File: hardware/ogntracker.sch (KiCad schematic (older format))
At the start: 53 parts, among them J1 ANT, J2 SWD, J3 BOOT, SW1 RESET, U1 LM2936-3.3, Y1 32.768K, Y2 8MHz

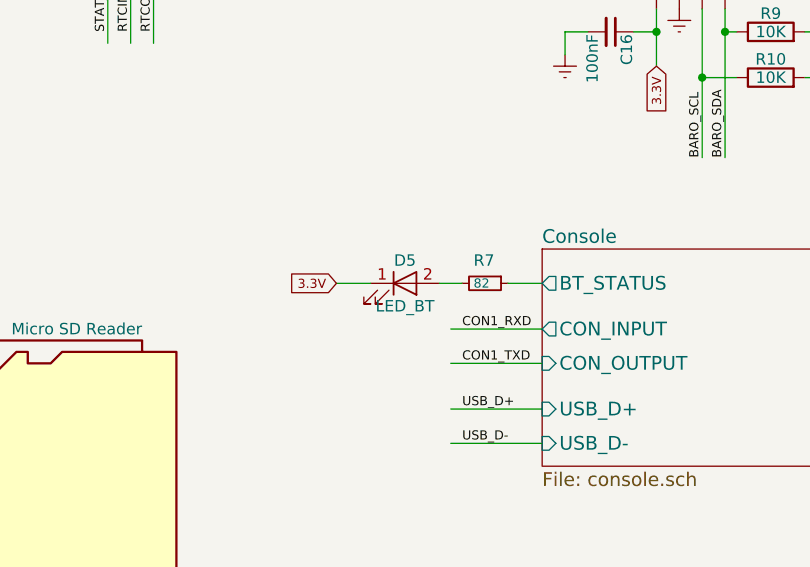
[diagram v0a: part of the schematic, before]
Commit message: All the used footprints moved to project directory
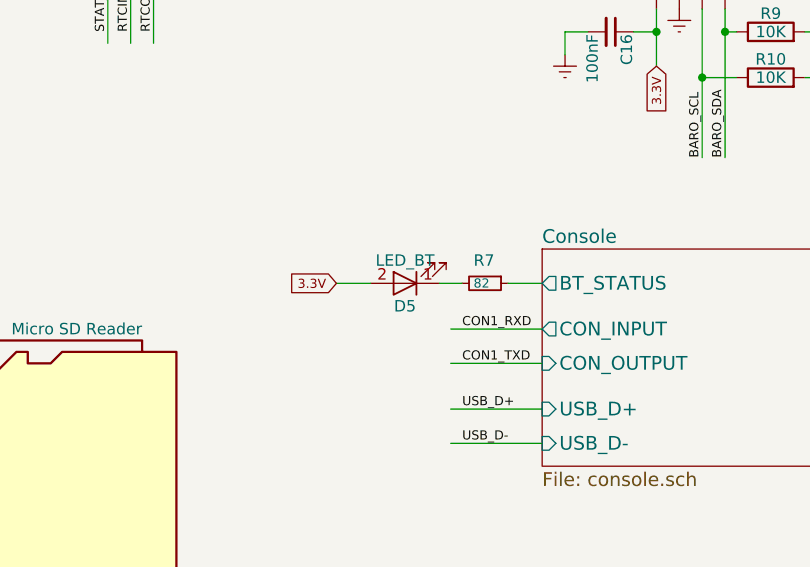
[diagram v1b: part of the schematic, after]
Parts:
- BARO1: footprint OGN Tracker:BMP280_HandSoldering -> KDR Tracker:BMP280
- D2, D5: footprint OGN Tracker:Molex_PicoBlade_02x1.25mm_HandSoldering -> KDR Tracker:Molex_PicoBlade_53047-0210_02x1.25mm_Straight
- J1: footprint OGN Tracker:IPEX -> KDR Tracker:IPEX
- PWR1: footprint OGN Tracker:Buck_Converter_Sm_HandSoldering -> KDR Tracker:Buck_Converter_Sm
- RF1: footprint OGN Tracker:RFM69HW -> KDR Tracker:RFM69HW
- SDCARD1: footprint OGN Tracker:SDCARD_BOMB -> KDR Tracker:SDCARD_BOMB
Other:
- moved on the sheet: D5
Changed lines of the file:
@@
 LIBS:switches
 LIBS:kedder
+LIBS:bt-hc-05
 LIBS:ogntracker-cache
 EELAYER 25 0
@@
 F 0 "RF1" H 2800 5600 60  0000 L CNN
 F 1 "RFM69HW" H 2700 4500 60  0000 C CNN
-F 2 "OGN Tracker:RFM69HW" H 2700 4950 60  0001 C CNN
+F 2 "KDR Tracker:RFM69HW" H 2700 4950 60  0001 C CNN
 F 3 "" H 2700 4950 60  0001 C CNN
 	1    2700 4950
@@
 F 0 "J1" H 1810 5670 50  0000 C CNN
 F 1 "ANT" V 1915 5550 50  0000 C CNN
-F 2 "OGN Tracker:IPEX" H 1800 5550 50  0001 C CNN
+F 2 "KDR Tracker:IPEX" H 1800 5550 50  0001 C CNN
 F 3 "" H 1800 5550 50  0001 C CNN
 	1    1800 5550
@@
 F 0 "BARO1" H 8850 4400 60  0000 C CNN
 F 1 "BMP280" H 8950 4100 60  0000 C CNN
-F 2 "OGN Tracker:BMP280_HandSoldering" H 9000 3750 60  0001 C CNN
+F 2 "KDR Tracker:BMP280" H 9000 3750 60  0001 C CNN
 F 3 "" H 9000 3750 60  0001 C CNN
 	1    8950 3950
@@
 F 0 "PWR1" H 1750 1700 60  0000 L CNN
 F 1 "BUCK_CVTR" H 2050 1600 40  0000 L CNN
-F 2 "OGN Tracker:Buck_Converter_Sm_HandSoldering" H 1800 1450 60  0001 C CNN
+F 2 "KDR Tracker:Buck_Converter_Sm" H 1800 1450 60  0001 C CNN
 F 3 "" H 1800 1450 60  0001 C CNN
 	1    2100 1450
@@
 F 0 "SDCARD1" H 5250 7150 50  0000 C CNN
 F 1 "Micro SD Reader" H 6550 7150 50  0000 R CNN
-F 2 "OGN Tracker:SDCARD_BOMB" H 7950 7150 50  0001 C CNN
+F 2 "KDR Tracker:SDCARD_BOMB" H 7950 7150 50  0001 C CNN
 F 3 "" H 5900 6550 50  0001 C CNN
 	1    5900 6450
@@
 F 0 "D5" H 7700 5650 50  0000 C CNN
 F 1 "LED_BT" H 7700 5450 50  0000 C CNN
-F 2 "OGN Tracker:Molex_PicoBlade_02x1.25mm_HandSoldering" H 7700 5550 50  0001 C CNN
+F 2 "KDR Tracker:Molex_PicoBlade_53047-0210_02x1.25mm_Straight" H 7700 5550 50  0001 C CNN
 F 3 "" H 7700 5550 50  0001 C CNN
 	1    7700 5550
-	1    0    0    -1
+	-1   0    0    1
 $EndComp
 Text GLabel 7400 5550 0    40   Input ~ 0
@@
 F 0 "D2" H 1800 7225 50  0000 L CNN
 F 1 "STATUS_PANEL" H 1675 7000 50  0000 L CNN
-F 2 "OGN Tracker:Molex_PicoBlade_02x1.25mm_HandSoldering" V 1850 7100 50  0001 C CNN
+F 2 "KDR Tracker:Molex_PicoBlade_53047-0210_02x1.25mm_Straight" V 1850 7100 50  0001 C CNN
 F 3 "" V 1850 7100 50  0001 C CNN
 	1    1850 7100

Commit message: v0.6 routed
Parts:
- removed C12, C13: 22pF, Capacitors_SMD:C_0603_HandSoldering, symbol C_Small
- removed J3: BOOT, Pin_Headers:Pin_Header_Straight_2x03_Pitch2.54mm, symbol CONN_02X03
- removed Y1: 32.768K, Crystals:Crystal_SMD_SeikoEpson_MC306-4pin_8.0x3.2mm, symbol Crystal_GND23_Small
- added J3: BOOT, Pin_Headers:Pin_Header_Straight_2x01_Pitch2.54mm, symbol CONN_01X02
- C14, C15: footprint Capacitors_SMD:C_0603_HandSoldering -> Capacitors_SMD:C_0603
- GPS1: footprint Pin_Headers:Pin_Header_Straight_1x06_Pitch2.00mm -> KDR Tracker:Molex_PicoBlade_53047-0610_06x1.25mm_Straight
- J1: footprint KDR Tracker:IPEX -> KDR Tracker:SMA_CONN
- LED1: renamed from D2; footprint KDR Tracker:Molex_PicoBlade_53047-0210_02x1.25mm_Straight -> LEDs:LED_D5.0mm_Horizontal_O3.81mm_Z3.0mm
- LED3: renamed from D5; footprint KDR Tracker:Molex_PicoBlade_53047-0210_02x1.25mm_Straight -> LEDs:LED_D5.0mm_Horizontal_O3.81mm_Z3.0mm
- Y2: footprint Crystals:Crystal_HC49-4H_Vertical -> Crystals:Crystal_SMD_HC49-SD
- renumbered D3 to LED2, D4 to LED5, CPU1 to MCU1
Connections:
- net labels added: Earth_Protective, RF_AUXSTAT, RF_IRQ, RF_RESET
- net labels removed: AUX_STATUS, CHIP_RESET, INT_REQ, USB_D+, USB_D-
- wire segments 186 -> 171
- no-connect marks 16 -> 18
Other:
- moved on the sheet: C10, C11, C14, C15, C8, C9, R8, Y2

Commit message: Components renamed to be more uniform
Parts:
- renumbered PWR1 to B1, BARO1 to B2, GPS1 to J8, SDCARD1 to J9
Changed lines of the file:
@@
 SPI_SELECT
 $Comp
-L VK2828U7G5LF GPS1
+L VK2828U7G5LF J8
 U 1 1 59822930
 P 1800 3500
-F 0 "GPS1" H 1400 3000 60  0000 L CNN
+F 0 "J8" H 1400 3000 60  0000 L CNN
 F 1 "VK2828U7G5LF" H 1800 3250 40  0000 C CNN
 F 2 "KDR Tracker:Molex_PicoBlade_53047-0610_06x1.25mm_Straight" H 2250 3700 40  0001 C CNN
@@
 GPS_ENABLE
 $Comp
-L Earth #PWR01
+L Earth #PWR7
 U 1 1 59824D08
 P 2250 5500
-F 0 "#PWR01" H 2250 5250 50  0001 C CNN
+F 0 "#PWR7" H 2250 5250 50  0001 C CNN
 F 1 "Earth" H 2250 5350 50  0001 C CNN
 F 2 "" H 2250 5500 50  0001 C CNN
@@
 $EndComp
 $Comp
-L Earth #PWR02
+L Earth #PWR6
 U 1 1 5983759C
 P 2200 2650
-F 0 "#PWR02" H 2200 2400 50  0001 C CNN
+F 0 "#PWR6" H 2200 2400 50  0001 C CNN
 F 1 "Earth" H 2200 2500 50  0001 C CNN
 F 2 "" H 2200 2650 50  0001 C CNN
@@
 $EndComp
 $Comp
-L Earth #PWR03
+L Earth #PWR4
 U 1 1 59838011
 P 1800 5750
-F 0 "#PWR03" H 1800 5500 50  0001 C CNN
+F 0 "#PWR4" H 1800 5500 50  0001 C CNN
 F 1 "Earth" H 1800 5600 50  0001 C CNN
 F 2 "" H 1800 5750 50  0001 C CNN
@@
 $EndComp
 $Comp
-L Earth #PWR04
+L Earth #PWR5
 U 1 1 59838B5F
 P 2100 1850
-F 0 "#PWR04" H 2100 1600 50  0001 C CNN
+F 0 "#PWR5" H 2100 1600 50  0001 C CNN
 F 1 "Earth" H 2100 1700 50  0001 C CNN
 F 2 "" H 2100 1850 50  0001 C CNN
@@
 $EndComp
 $Comp
-L +12V #PWR05
+L +12V #PWR1
 U 1 1 59838C1F
 P 850 900
-F 0 "#PWR05" H 850 750 50  0001 C CNN
+F 0 "#PWR1" H 850 750 50  0001 C CNN
 F 1 "+12V" H 850 1040 50  0000 C CNN
 F 2 "" H 850 900 50  0001 C CNN
@@
 5V
 $Comp
-L Earth #PWR06
+L Earth #PWR9
 U 1 1 59970B11
 P 3200 5800
-F 0 "#PWR06" H 3200 5550 50  0001 C CNN
+F 0 "#PWR9" H 3200 5550 50  0001 C CNN
 F 1 "Earth" H 3200 5650 50  0001 C CNN
 F 2 "" H 3200 5800 50  0001 C CNN
@@
 3.3V
 $Comp
-L BMP280 BARO1
+L BMP280 B2
 U 1 1 59B17E39
 P 8950 3950
-F 0 "BARO1" H 8850 4400 60  0000 C CNN
+F 0 "B2" H 8850 4400 60  0000 C CNN
 F 1 "BMP280" H 8950 4100 60  0000 C CNN
 F 2 "KDR Tracker:BMP280" H 9000 3750 60  0001 C CNN
@@
 3.3V
 $Comp
-L Earth #PWR07
+L Earth #PWR24
 U 1 1 59B181A3
 P 8900 4350
-F 0 "#PWR07" H 8900 4100 50  0001 C CNN
+F 0 "#PWR24" H 8900 4100 50  0001 C CNN
 F 1 "Earth" H 8900 4200 50  0001 C CNN
 F 2 "" H 8900 4350 50  0001 C CNN
@@
 $EndComp
 $Comp
-L BUCK_CVTR PWR1
+L BUCK_CVTR B1
 U 1 1 59B305A7
 P 2100 1450
-F 0 "PWR1" H 1750 1700 60  0000 L CNN
+F 0 "B1" H 1750 1700 60  0000 L CNN
 F 1 "BUCK_CVTR" H 2050 1600 40  0000 L CNN
 F 2 "KDR Tracker:Buck_Converter_Sm" H 1800 1450 60  0001 C CNN
@@
 NoConn ~ 1650 1550
 $Comp
-L Earth #PWR08
+L Earth #PWR23
 U 1 1 59B420DC
 P 8400 4550
-F 0 "#PWR08" H 8400 4300 50  0001 C CNN
+F 0 "#PWR23" H 8400 4300 50  0001 C CNN
 F 1 "Earth" H 8400 4400 50  0001 C CNN
 F 2 "" H 8400 4550 50  0001 C CNN
@@
 $EndComp
 $Comp
-L Earth #PWR09
+L Earth #PWR11
 U 1 1 59B6DC4B
 P 3550 5800
-F 0 "#PWR09" H 3550 5550 50  0001 C CNN
+F 0 "#PWR11" H 3550 5550 50  0001 C CNN
 F 1 "Earth" H 3550 5650 50  0001 C CNN
 F 2 "" H 3550 5800 50  0001 C CNN
@@
 $EndComp
 $Comp
-L Earth #PWR010
+L Earth #PWR2
 U 1 1 59B6EDC9
 P 1600 800
-F 0 "#PWR010" H 1600 550 50  0001 C CNN
+F 0 "#PWR2" H 1600 550 50  0001 C CNN
 F 1 "Earth" H 1600 650 50  0001 C CNN
 F 2 "" H 1600 800 50  0001 C CNN
@@
 $EndComp
 $Comp
-L Micro_SD_Card_Det1 SDCARD1
+L Micro_SD_Card_Det1 J9
 U 1 1 5A00BEEF
 P 5900 6450
-F 0 "SDCARD1" H 5250 7150 50  0000 C CNN
+F 0 "J9" H 5250 7150 50  0000 C CNN
 F 1 "Micro SD Reader" H 6550 7150 50  0000 R CNN
 F 2 "KDR Tracker:SDCARD_BOMB" H 7950 7150 50  0001 C CNN
@@
 $EndComp
 $Comp
-L Earth #PWR011
+L Earth #PWR15
 U 1 1 5A00C4B3
 P 4900 7100
-F 0 "#PWR011" H 4900 6850 50  0001 C CNN
+F 0 "#PWR15" H 4900 6850 50  0001 C CNN
 F 1 "Earth" H 4900 6950 50  0001 C CNN
 F 2 "" H 4900 7100 50  0001 C CNN
@@
 3.3V
 $Comp
-L Earth #PWR012
+L Earth #PWR17
 U 1 1 5A00D319
 P 5400 5550
-F 0 "#PWR012" H 5400 5300 50  0001 C CNN
+F 0 "#PWR17" H 5400 5300 50  0001 C CNN
 F 1 "Earth" H 5400 5400 50  0001 C CNN
 F 2 "" H 5400 5550 50  0001 C CNN
@@
 BUZ_IN
 $Comp
-L Earth #PWR013
+L Earth #PWR10
 U 1 1 5A023604
 P 3400 1850
-F 0 "#PWR013" H 3400 1600 50  0001 C CNN
+F 0 "#PWR10" H 3400 1600 50  0001 C CNN
 F 1 "Earth" H 3400 1700 50  0001 C CNN
 F 2 "" H 3400 1850 50  0001 C CNN
@@
 $EndComp
 $Comp
-L Earth #PWR014
+L Earth #PWR12
 U 1 1 5A023990
 P 3750 1850
-F 0 "#PWR014" H 3750 1600 50  0001 C CNN
+F 0 "#PWR12" H 3750 1600 50  0001 C CNN
 F 1 "Earth" H 3750 1700 50  0001 C CNN
 F 2 "" H 3750 1850 50  0001 C CNN
@@
 $EndComp
 $Comp
-L Earth #PWR015
+L Earth #PWR8
 U 1 1 5A0243BD
 P 3000 1850
-F 0 "#PWR015" H 3000 1600 50  0001 C CNN
+F 0 "#PWR8" H 3000 1600 50  0001 C CNN
 F 1 "Earth" H 3000 1700 50  0001 C CNN
 F 2 "" H 3000 1850 50  0001 C CNN
@@
 $EndComp
 $Comp
-L Earth #PWR016
+L Earth #PWR19
 U 1 1 5A19EFEA
 P 5700 4400
-F 0 "#PWR016" H 5700 4150 50  0001 C CNN
+F 0 "#PWR19" H 5700 4150 50  0001 C CNN
 F 1 "Earth" H 5700 4250 50  0001 C CNN
 F 2 "" H 5700 4400 50  0001 C CNN
@@
 $EndComp
 $Comp
-L Earth #PWR017
+L Earth #PWR16
 U 1 1 5A1A0E87
 P 5350 1000
-F 0 "#PWR017" H 5350 750 50  0001 C CNN
+F 0 "#PWR16" H 5350 750 50  0001 C CNN
 F 1 "Earth" H 5350 850 50  0001 C CNN
 F 2 "" H 5350 1000 50  0001 C CNN
@@
 $EndComp
 $Comp
-L Earth #PWR018
+L Earth #PWR25
 U 1 1 5A1A7425
 P 9400 1650
-F 0 "#PWR018" H 9400 1400 50  0001 C CNN
+F 0 "#PWR25" H 9400 1400 50  0001 C CNN
 F 1 "Earth" H 9400 1500 50  0001 C CNN
 F 2 "" H 9400 1650 50  0001 C CNN
@@
 $EndComp
 $Comp
-L Earth #PWR019
+L Earth #PWR13
 U 1 1 5A1B01CE
 P 4100 2050
-F 0 "#PWR019" H 4100 1800 50  0001 C CNN
+F 0 "#PWR13" H 4100 1800 50  0001 C CNN
 F 1 "Earth" H 4100 1900 50  0001 C CNN
 F 2 "" H 4100 2050 50  0001 C CNN
@@
 $EndComp
 $Comp
-L Earth #PWR020
+L Earth #PWR3
 U 1 1 5A1B2252
 P 1650 2500
-F 0 "#PWR020" H 1650 2250 50  0001 C CNN
+F 0 "#PWR3" H 1650 2250 50  0001 C CNN
 F 1 "Earth" H 1650 2350 50  0001 C CNN
 F 2 "" H 1650 2500 50  0001 C CNN
@@
 NoConn ~ 4900 3700
 $Comp
-L Earth #PWR021
+L Earth #PWR21
 U 1 1 5A1C547E
 P 6750 7000
-F 0 "#PWR021" H 6750 6750 50  0001 C CNN
+F 0 "#PWR21" H 6750 6750 50  0001 C CNN
 F 1 "Earth" H 6750 6850 50  0001 C CNN
 F 2 "" H 6750 7000 50  0001 C CNN
@@
 $EndComp
 $Comp
-L Earth #PWR022
+L Earth #PWR26
 U 1 1 5A2F0D34
 P 10450 2750
-F 0 "#PWR022" H 10450 2500 50  0001 C CNN
+F 0 "#PWR26" H 10450 2500 50  0001 C CNN
 F 1 "Earth" H 10450 2600 50  0001 C CNN
 F 2 "" H 10450 2750 50  0001 C CNN
@@
 	5600 4200 5600 4500
 $Comp
-L Earth_Protective #PWR023
+L Earth_Protective #PWR18
 U 1 1 5A304E47
 P 5600 4500
-F 0 "#PWR023" H 5850 4250 50  0001 C CNN
+F 0 "#PWR18" H 5850 4250 50  0001 C CNN
 F 1 "Earth_Protective" H 6050 4350 50  0001 C CNN
 F 2 "" H 5600 4400 50  0001 C CNN
@@
 $EndComp
 $Comp
-L Earth_Protective #PWR024
+L Earth_Protective #PWR22
 U 1 1 5A3051F7
 P 7550 1550
-F 0 "#PWR024" H 7800 1300 50  0001 C CNN
+F 0 "#PWR22" H 7800 1300 50  0001 C CNN
 F 1 "Earth_Protective" H 8000 1400 50  0001 C CNN
 F 2 "" H 7550 1450 50  0001 C CNN
@@
 	5700 4250 5900 4250
 $Comp
-L Earth #PWR025
+L Earth #PWR27
 U 1 1 5A3090AA
 P 10700 1650
-F 0 "#PWR025" H 10700 1400 50  0001 C CNN
+F 0 "#PWR27" H 10700 1400 50  0001 C CNN
 F 1 "Earth" H 10700 1500 50  0001 C CNN
 F 2 "" H 10700 1650 50  0001 C CNN
@@
 3.3V
 $Comp
-L Earth #PWR026
+L Earth #PWR14
 U 1 1 5A3180D8
 P 4900 1850
-F 0 "#PWR026" H 4900 1600 50  0001 C CNN
+F 0 "#PWR14" H 4900 1600 50  0001 C CNN
 F 1 "Earth" H 4900 1700 50  0001 C CNN
 F 2 "" H 4900 1850 50  0001 C CNN
@@
 	4900 1800 4900 1850
 $Comp
-L Earth_Protective #PWR027
+L Earth_Protective #PWR20
 U 1 1 5A31B6EF
 P 6600 4500
-F 0 "#PWR027" H 6850 4250 50  0001 C CNN
+F 0 "#PWR20" H 6850 4250 50  0001 C CNN
 F 1 "Earth_Protective" H 7050 4350 50  0001 C CNN
 F 2 "" H 6600 4400 50  0001 C CNN
